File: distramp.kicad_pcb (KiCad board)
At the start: 4 copper layers, 50 x 50 mm, 28 parts, among them P1 ANT, P2 OUT, P3 OUT, P4 OUT, P5 OUT, P6 PWR, U1 MAAL-010704, U2 TPS796xxDCQ

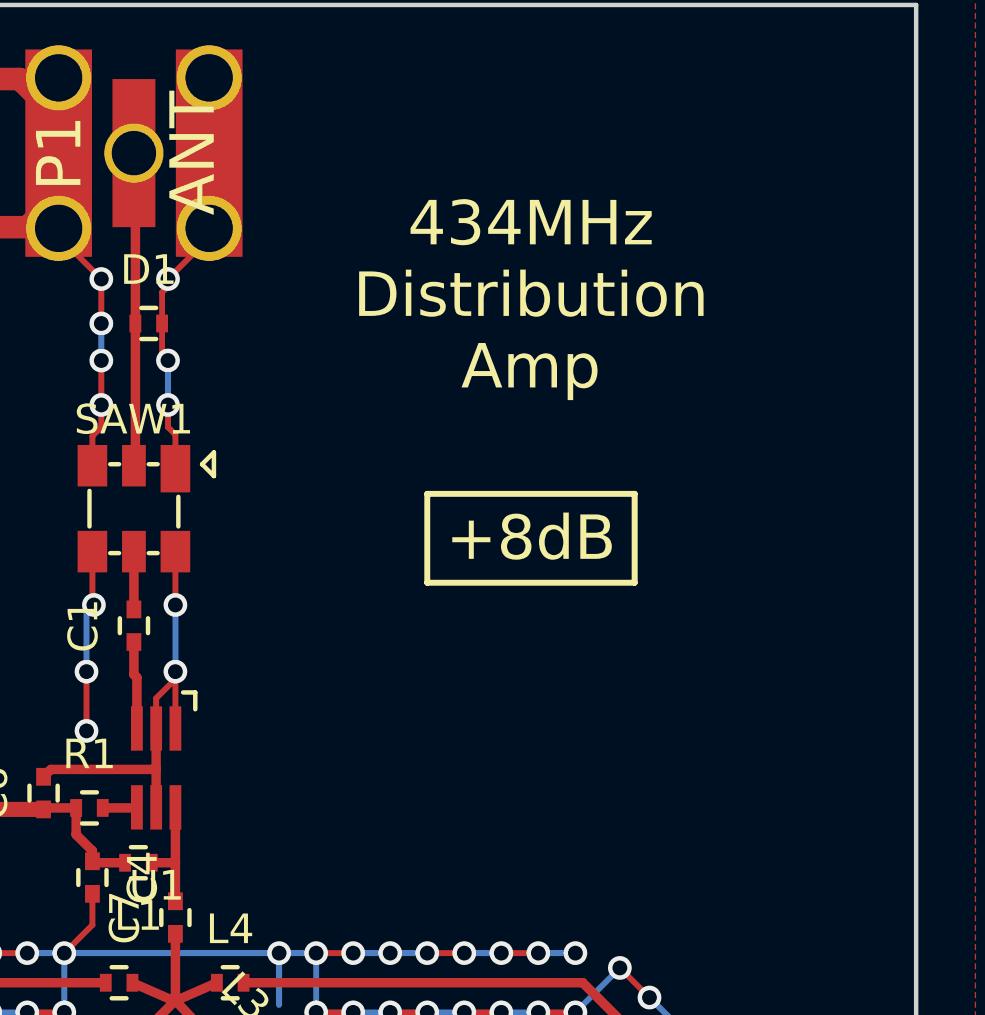
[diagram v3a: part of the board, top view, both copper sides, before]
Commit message: Specify 869MHz component values
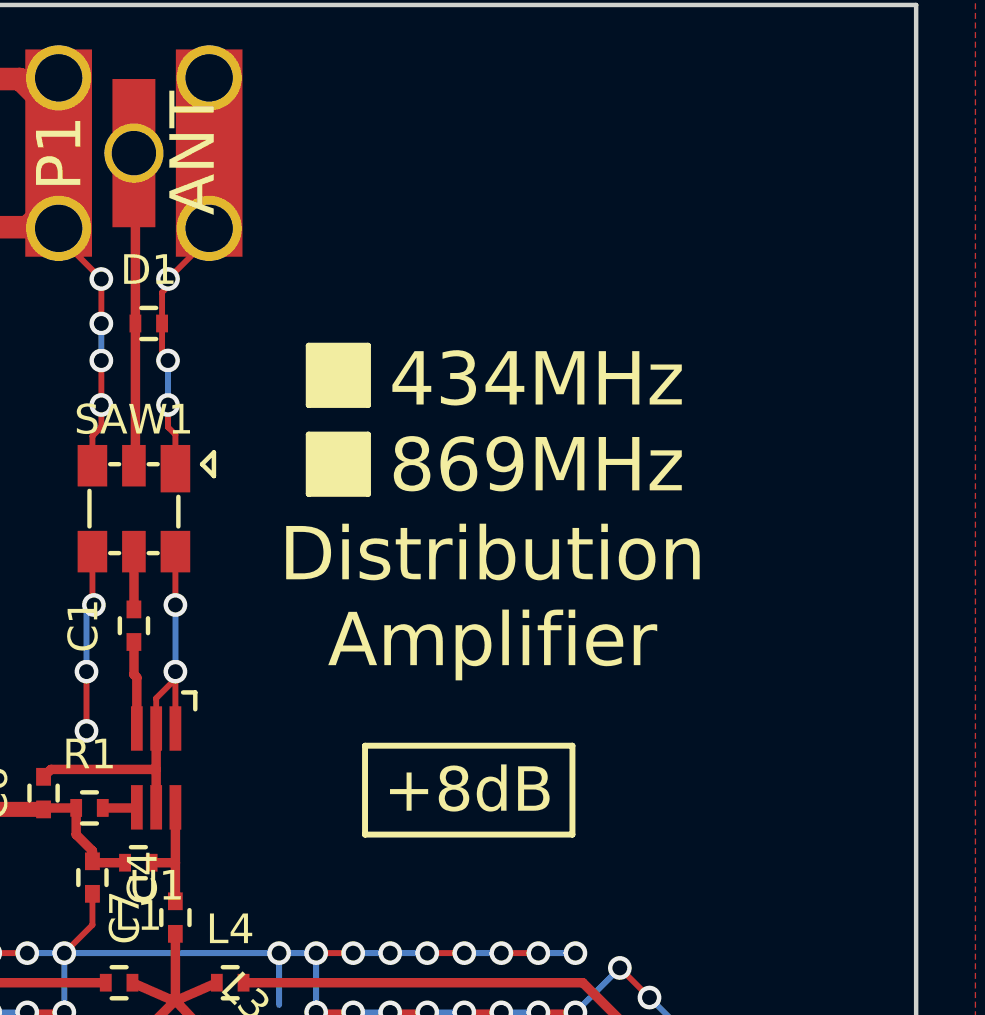
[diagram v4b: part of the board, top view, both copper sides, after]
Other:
- rule pad_to_mask_clearance: 0.2 -> 0
- board text added: "434MHz 869MHz"
- board text added: "Distribution Amplifier"
- board text removed: "434MHz Distribution Amp"
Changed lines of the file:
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@@
     (area 59.924999 59.924999 110.075001 110.075001)
     (thickness 1.6)
-    (drawings 14)
+    (drawings 23)
     (tracks 354)
     (zones 0)
@@
   )
   (setup
-    (last_trace_width 0.32)
+    (last_trace_width 0.15)
     (user_trace_width 0.18)
     (user_trace_width 0.2)
@@
     (pad_size 1.524 1.524)
     (pad_drill 0.762)
-    (pad_to_mask_clearance 0.2)
+    (pad_to_mask_clearance 0)
     (aux_axis_origin 0 0)
     (visible_elements FFFFFF7F)
     (pcbplotparams
-      (layerselection 0x00030_80000001)
+      (layerselection 0x000f0_80000007)
       (usegerberextensions false)
       (excludeedgelayer true)
@@
       (outputformat 1)
       (mirror false)
-      (drillshape 1)
+      (drillshape 0)
       (scaleselection 1)
       (outputdirectory ""))
@@
     )
   )
+  (gr_text "Distribution\nAmplifier" (at 95.7 80) (layer F.SilkS)
+    (effects (font (size 1.8 1.8) (thickness 0.3)))
+  )
+  (gr_line (start 91.5 71.5) (end 89.5 71.5) (angle 90) (layer F.SilkS) (width 0.2))
+  (gr_line (start 91.5 71.5) (end 91.5 73.5) (angle 90) (layer F.SilkS) (width 0.2))
+  (gr_line (start 89.5 73.5) (end 89.5 71.5) (angle 90) (layer F.SilkS) (width 0.2))
+  (gr_line (start 91.5 73.5) (end 89.5 73.5) (angle 90) (layer F.SilkS) (width 0.2))
+  (gr_line (start 91.5 74.5) (end 91.5 76.5) (angle 90) (layer F.SilkS) (width 0.2))
+  (gr_line (start 89.5 74.5) (end 91.5 74.5) (angle 90) (layer F.SilkS) (width 0.2))
+  (gr_line (start 89.5 76.5) (end 89.5 74.5) (angle 90) (layer F.SilkS) (width 0.2))
+  (gr_line (start 91.5 76.5) (end 89.5 76.5) (angle 90) (layer F.SilkS) (width 0.2))
   (gr_text 5V (at 65 70.5) (layer F.SilkS)
     (effects (font (size 1.5 1.5) (thickness 0.3)))
   )
-  (gr_line (start 93.5 76.5) (end 93.5 79.5) (angle 90) (layer F.SilkS) (width 0.2))
-  (gr_line (start 100.5 76.5) (end 93.5 76.5) (angle 90) (layer F.SilkS) (width 0.2))
-  (gr_line (start 100.5 79.5) (end 100.5 76.5) (angle 90) (layer F.SilkS) (width 0.2))
-  (gr_line (start 93.5 79.5) (end 100.5 79.5) (angle 90) (layer F.SilkS) (width 0.2))
-  (gr_text +8dB (at 97 78) (layer F.SilkS)
+  (gr_line (start 91.4 85) (end 91.4 88) (angle 90) (layer F.SilkS) (width 0.2))
+  (gr_line (start 98.4 85) (end 91.4 85) (angle 90) (layer F.SilkS) (width 0.2))
+  (gr_line (start 98.4 88) (end 98.4 85) (angle 90) (layer F.SilkS) (width 0.2))
+  (gr_line (start 91.4 88) (end 98.4 88) (angle 90) (layer F.SilkS) (width 0.2))
+  (gr_text +8dB (at 94.9 86.5) (layer F.SilkS)
     (effects (font (size 1.5 1.5) (thickness 0.3)))
   )
@@
   (gr_line (start 62 66.25) (end 62 67.75) (angle 90) (layer F.SilkS) (width 0.2))
   (gr_line (start 61.25 67) (end 62.75 67) (angle 90) (layer F.SilkS) (width 0.2))
-  (gr_text "434MHz\nDistribution\nAmp" (at 97 69.8) (layer F.SilkS)
-    (effects (font (size 1.5 1.5) (thickness 0.3)))
+  (gr_text "434MHz\n869MHz\n" (at 97.2 74.1) (layer F.SilkS)
+    (effects (font (size 1.8 1.8) (thickness 0.3)))
   )
   (gr_line (start 60 110) (end 110 110) (angle 90) (layer Edge.Cuts) (width 0.15))
@@
   (segment (start 83.6 80.4) (end 83.6 78.45) (width 0.32) (layer F.Cu) (net 2))
   (segment (start 68.75 72.575) (end 68.75 69.5) (width 0.32) (layer F.Cu) (net 3))
-  (segment (start 66.25 67) (end 65 67) (width 0.32) (layer F.Cu) (net 3) (status 800000))
+  (segment (start 66.25 67) (end 65 67) (width 0.32) (layer F.Cu) (net 3))
   (segment (start 68.75 69.5) (end 66.25 67) (width 0.32) (layer F.Cu) (net 3))
   (segment (start 70.93 69.7) (end 70.93 71.02) (width 0.508) (layer F.Cu) (net 3))
@@
   (segment (start 68.75 72.575) (end 68.75 73.5) (width 0.508) (layer F.Cu) (net 3))
   (segment (start 69.66 71.665) (end 68.75 72.575) (width 0.508) (layer F.Cu) (net 3))
-  (segment (start 70.75 73.5) (end 71.5 73.5) (width 0.762) (layer F.Cu) (net 4) (status 400000))
+  (segment (start 70.75 73.5) (end 71.5 73.5) (width 0.762) (layer F.Cu) (net 4))
   (segment (start 71.5 73.5) (end 72.2 72.8) (width 0.762) (layer F.Cu) (net 4))
-  (segment (start 72.2 69.7) (end 72.2 72.8) (width 0.762) (layer F.Cu) (net 4) (status 400000))
+  (segment (start 72.2 69.7) (end 72.2 72.8) (width 0.762) (layer F.Cu) (net 4))
   (segment (start 72.2 72.8) (end 72.2 72.95) (width 0.762) (layer F.Cu) (net 4))
-  (segment (start 72.2 72.95) (end 72.75 73.5) (width 0.762) (layer F.Cu) (net 4) (status 800000))
-  (segment (start 81.06 65) (end 81.06 66.44) (width 0.762) (layer F.Cu) (net 4) (status C00000))
-  (segment (start 81.06 66.44) (end 80 67.5) (width 0.762) (layer F.Cu) (net 4) (status C00000))
-  (segment (start 80 67.5) (end 76.75 67.5) (width 0.762) (layer F.Cu) (net 4) (status 400000))
+  (segment (start 72.2 72.95) (end 72.75 73.5) (width 0.762) (layer F.Cu) (net 4))
+  (segment (start 81.06 65) (end 81.06 66.44) (width 0.762) (layer F.Cu) (net 4))
+  (segment (start 81.06 66.44) (end 80 67.5) (width 0.762) (layer F.Cu) (net 4))
+  (segment (start 80 67.5) (end 76.75 67.5) (width 0.762) (layer F.Cu) (net 4))
   (segment (start 76.75 67.5) (end 76 66.75) (width 0.762) (layer F.Cu) (net 4))
   (segment (start 76 66.75) (end 72.25 66.75) (width 0.762) (layer F.Cu) (net 4))
   (segment (start 72.25 66.75) (end 72.2 66.8) (width 0.762) (layer F.Cu) (net 4))
-  (segment (start 72.2 66.8) (end 72.2 69.7) (width 0.762) (layer F.Cu) (net 4) (status 800000))
-  (segment (start 81.06 65) (end 81.06 63.81) (width 0.762) (layer F.Cu) (net 4) (status C00000))
-  (segment (start 81.06 63.81) (end 79.75 62.5) (width 0.762) (layer F.Cu) (net 4) (status 400000))
-  (segment (start 74.75 63.5) (end 72.2 63.5) (width 0.762) (layer F.Cu) (net 4) (status 800000))
+  (segment (start 72.2 66.8) (end 72.2 69.7) (width 0.762) (layer F.Cu) (net 4))
+  (segment (start 81.06 65) (end 81.06 63.81) (width 0.762) (layer F.Cu) (net 4))
+  (segment (start 81.06 63.81) (end 79.75 62.5) (width 0.762) (layer F.Cu) (net 4))
+  (segment (start 74.75 63.5) (end 72.2 63.5) (width 0.762) (layer F.Cu) (net 4))
   (segment (start 75.75 62.5) (end 74.75 63.5) (width 0.762) (layer F.Cu) (net 4))
   (segment (start 79.75 62.5) (end 75.75 62.5) (width 0.762) (layer F.Cu) (net 4))
-  (segment (start 65 64.46) (end 67.54 64.46) (width 0.762) (layer F.Cu) (net 4) (status 400000))
-  (segment (start 68.5 63.5) (end 72.2 63.5) (width 0.762) (layer F.Cu) (net 4) (status 800000))
+  (segment (start 65 64.46) (end 67.54 64.46) (width 0.762) (layer F.Cu) (net 4))
+  (segment (start 68.5 63.5) (end 72.2 63.5) (width 0.762) (layer F.Cu) (net 4))
   (segment (start 67.54 64.46) (end 68.5 63.5) (width 0.762) (layer F.Cu) (net 4))
   (segment (start 61 106) (end 61 101.2) (width 0.508) (layer F.Cu) (net 4))
@@
   (segment (start 74.95 71.475) (end 75.35 71.475) (width 0.2) (layer F.Cu) (net 5))
   (segment (start 74.74 71.265) (end 74.95 71.475) (width 0.2) (layer F.Cu) (net 5))
-  (segment (start 74.75 73.5) (end 74.75 78) (width 0.32) (layer F.Cu) (net 6) (status 400000))
-  (segment (start 73.12 79.63) (end 73.12 86) (width 0.32) (layer F.Cu) (net 6) (status 800000))
+  (segment (start 74.75 73.5) (end 74.75 78) (width 0.32) (layer F.Cu) (net 6))
+  (segment (start 73.12 79.63) (end 73.12 86) (width 0.32) (layer F.Cu) (net 6))
   (segment (start 74.75 78) (end 73.12 79.63) (width 0.32) (layer F.Cu) (net 6))
   (segment (start 80.55 87.15) (end 78.15 87.15) (width 0.508) (layer F.Cu) (net 6))
@@
       )
     )
+  )
+  (zone (net 0) (net_name "") (layer F.SilkS) (hatch edge 0.508)
+    (connect_pads (clearance 0.254))
+    (min_thickness 0.254)
+    (fill yes (arc_segments 16) (thermal_gap 0.508) (thermal_bridge_width 0.508))
+    (polygon
+      (pts
+        (xy 89.5 71.5) (xy 91.5 71.5) (xy 91.5 73.5) (xy 89.5 73.5)
+      )
+    )
+  )
+  (zone (net 0) (net_name "") (layer F.SilkS) (hatch edge 0.508)
+    (connect_pads (clearance 0.254))
+    (min_thickness 0.254)
+    (fill yes (arc_segments 16) (thermal_gap 0.508) (thermal_bridge_width 0.508))
+    (polygon
+      (pts
+        (xy 89.5 74.5) (xy 89.5 76.5) (xy 91.5 76.5) (xy 91.5 74.5)
+      )
+    )
